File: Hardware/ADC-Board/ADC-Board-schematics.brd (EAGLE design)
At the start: 80 x 50 mm, 20 parts

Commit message: layouts
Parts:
- removed CDCS502: CDCS502, components:SSOP-8
- removed IC6: (no value), SparkFun-PowerIC:SOT23-5
- added U$1: CDCS502TSSOP-8, components:TSSOP-8
- added U1: (no value), SparkFun-PowerIC:SOT223
- C28: value (none) -> 10uF
- moved TLV71333 5.08 mm to (18.7, 18.7)
- moved C27 5.08 mm to (14.2, 18.8)
- moved JP1 5.08 mm to (10.2, 25.4)
- moved C28 5.08 mm to (16.7, 25.8)
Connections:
- net +12VDC: now also U1.3; no longer IC6.3, IC6.4
- net 3V3: now also U$1.7; no longer CDCS502.7
- net 5VCC: now also U1.2, U1.4; no longer IC6.5
- net GND: now also U$1.2, U$1.3, U$1.4, U$1.5, U1.1; no longer CDCS502.2, CDCS502.3, CDCS502.4, CDCS502.5, IC6.2
- net N$29: now also U$1.1; no longer CDCS502.1
- net N$30: now also U$1.8; no longer CDCS502.8
- net N$32: now also U$1.6; no longer CDCS502.6
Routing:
- net 3V3: track 42.3 -> 48.9 mm
- net GND: track 205.3 -> 210.8 mm
- net 5VCC: track 18.8 -> 24.0 mm
- net 5VCON: track 11.8 -> 16.1 mm
- net N$30: track 6.68 -> 8.62 mm
- net N$32: track 12.6 -> 11.1 mm
- net +12VDC: track 10.8 -> 9.75 mm

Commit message: tvs considerations
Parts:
- added D1, D2, D3, D4, D5: (no value), diode:DO-214AC
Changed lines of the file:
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@@
 </element>
 <element name="U$1" library="components" package="TSSOP-8" value="CDCS502TSSOP-8" x="45.42" y="13.57" rot="R180"/>
+<element name="D1" library="diode" package="DO-214AC" value="" x="9.51" y="5.79"/>
+<element name="D2" library="diode" package="DO-214AC" value="" x="3.81" y="-3.81"/>
+<element name="D3" library="diode" package="DO-214AC" value="" x="3.81" y="-8.89"/>
+<element name="D4" library="diode" package="DO-214AC" value="" x="3.81" y="-13.97"/>
+<element name="D5" library="diode" package="DO-214AC" value="" x="3.81" y="-19.05"/>
 </elements>
 <signals>

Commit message: adc-board
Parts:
- moved JP1 24.3 mm to (-6.35, 7.62)
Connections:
- net 5VCC: now also C27.1, TLV71333.1, TLV71333.3
- net 5VCON: no longer C27.1, TLV71333.1, TLV71333.3
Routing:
- net GND: track 210.8 -> 169.2 mm
- net 5VCON: track 16.1 -> 3.69 mm
- net +12VDC: track 9.75 -> 4.40 mm
- net 5VCC: track 24.0 -> 28.2 mm
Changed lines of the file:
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@@
 <layer number="14" name="Route14" color="1" fill="6" visible="no" active="no"/>
 <layer number="15" name="Route15" color="4" fill="6" visible="no" active="no"/>
-<layer number="16" name="Bottom" color="1" fill="1" visible="no" active="yes"/>
+<layer number="16" name="Bottom" color="1" fill="1" visible="yes" active="yes"/>
 <layer number="17" name="Pads" color="2" fill="1" visible="yes" active="yes"/>
 <layer number="18" name="Vias" color="2" fill="1" visible="yes" active="yes"/>
@@
 <layer number="24" name="bOrigins" color="15" fill="1" visible="yes" active="yes"/>
 <layer number="25" name="tNames" color="7" fill="1" visible="yes" active="yes"/>
-<layer number="26" name="bNames" color="7" fill="1" visible="no" active="yes"/>
+<layer number="26" name="bNames" color="7" fill="1" visible="yes" active="yes"/>
 <layer number="27" name="tValues" color="7" fill="1" visible="no" active="yes"/>
 <layer number="28" name="bValues" color="7" fill="1" visible="no" active="yes"/>
@@
 <element name="JP4" library="pinhead" package="2X02" value="" x="68.58" y="34.29" rot="R270"/>
 <element name="PCM1808" library="Pekkas_libraries" package="R-PDSO-G14" value="PCM1808PW" x="46.99" y="22.86"/>
-<element name="JP1" library="pinhead" package="2X02" value="" x="10.16" y="25.4"/>
+<element name="JP1" library="pinhead" package="2X02" value="" x="-6.35" y="7.62"/>
 <element name="TLV71333" library="Pekkas_libraries" package="SOT23-5" value="TVL713" x="18.74" y="18.68" rot="R270"/>
 <element name="C1" library="rcl" package="C0603" value="0.1uF" x="45.7" y="16.81"/>
@@
 <wire x1="47.85" y1="32.89" x2="47.72" y2="33.02" width="0.8128" layer="1"/>
 <contactref element="JP1" pad="4"/>
-<wire x1="11.43" y1="26.67" x2="13.12" y2="26.67" width="1.6764" layer="1"/>
-<wire x1="13.12" y1="26.67" x2="13.77" y2="27.32" width="1.6764" layer="1"/>
-<wire x1="13.77" y1="27.32" x2="13.97" y2="27.32" width="1.6764" layer="1"/>
-<wire x1="13.97" y1="27.32" x2="16.56" y2="27.32" width="1.6764" layer="1"/>
-<wire x1="34.29" y1="29.94" x2="21.59" y2="29.94" width="1.6764" layer="1"/>
-<wire x1="21.59" y1="29.94" x2="16.59" y2="29.94" width="1.6764" layer="1"/>
-<wire x1="16.59" y1="29.94" x2="13.97" y2="27.32" width="1.6764" layer="1"/>
 <contactref element="JP1" pad="2"/>
-<wire x1="11.43" y1="26.67" x2="8.89" y2="26.67" width="1.6764" layer="1"/>
+<wire x1="-5.08" y1="8.89" x2="-7.62" y2="8.89" width="1.6764" layer="1"/>
 <wire x1="14.19" y1="17.94" x2="14.13" y2="17.94" width="0.8128" layer="1"/>
 <wire x1="14.13" y1="17.94" x2="13.97" y2="17.78" width="0.8128" layer="1"/>
@@
 <wire x1="12.93" y1="17.78" x2="12.77" y2="17.62" width="1" layer="1"/>
 <wire x1="12.77" y1="17.62" x2="7.78" y2="17.62" width="1.6764" layer="1"/>
-<wire x1="7.78" y1="17.62" x2="5.08" y2="20.32" width="1.6764" layer="1"/>
-<wire x1="5.08" y1="20.32" x2="5.08" y2="25.4" width="1.6764" layer="1"/>
-<wire x1="5.08" y1="25.4" x2="6.35" y2="26.67" width="1.6764" layer="1"/>
-<wire x1="6.35" y1="26.67" x2="8.89" y2="26.67" width="1.6764" layer="1"/>
 <wire x1="17.4399" y1="18.68" x2="15.93" y2="18.68" width="0.55" layer="1"/>
 <wire x1="15.93" y1="18.68" x2="15.17" y2="17.92" width="0.55" layer="1"/>
@@
 <contactref element="U1" pad="1"/>
 <contactref element="C28" pad="2"/>
-<wire x1="21.0312" y1="28.9814" x2="21.59" y2="28.9814" width="0.4064" layer="1"/>
-<wire x1="21.59" y1="28.9814" x2="21.59" y2="29.94" width="0.4064" layer="1"/>
 <wire x1="14.19" y1="17.94" x2="14.19" y2="17.56" width="1.016" layer="1"/>
 <wire x1="14.19" y1="17.56" x2="16.51" y2="15.24" width="1.016" layer="1"/>
@@
 <wire x1="48.295" y1="14.545" x2="48.295" y2="16.765" width="0.6096" layer="1"/>
 <wire x1="48.295" y1="16.765" x2="48.35" y2="16.82" width="0.6096" layer="1"/>
-<wire x1="16.56" y1="27.32" x2="16.66" y2="27.22" width="0" layer="19" extent="1-1"/>
+<wire x1="16.66" y1="27.22" x2="21.0312" y2="28.9814" width="0" layer="19" extent="1-1"/>
+<wire x1="17.4399" y1="18.68" x2="16.66" y2="27.22" width="0" layer="19" extent="1-1"/>
+<wire x1="27.94" y1="17.78" x2="27.66" y2="18.01" width="0" layer="19" extent="1-1"/>
+<wire x1="-5.08" y1="8.89" x2="7.78" y2="17.62" width="0" layer="19" extent="1-1"/>
 </signal>
 <signal name="+12VDC">
 <contactref element="C28" pad="1"/>
 <contactref element="JP1" pad="3"/>
-<wire x1="11.43" y1="24.13" x2="16.37" y2="24.13" width="1.6764" layer="1"/>
-<wire x1="16.37" y1="24.13" x2="16.66" y2="24.42" width="1.6764" layer="1"/>
 <contactref element="U1" pad="3"/>
 <wire x1="21.0312" y1="24.3586" x2="16.7214" y2="24.3586" width="1.27" layer="1"/>
 <wire x1="16.7214" y1="24.3586" x2="16.66" y2="24.42" width="1.27" layer="1"/>
+<wire x1="-5.08" y1="6.35" x2="16.7214" y2="24.3586" width="0" layer="19" extent="1-1"/>
 </signal>
 <signal name="5VCON">
-<contactref element="C27" pad="1"/>
-<contactref element="TLV71333" pad="1"/>
-<contactref element="TLV71333" pad="3"/>
 <contactref element="JP1" pad="1"/>
-<wire x1="8.89" y1="24.13" x2="8.89" y2="22.86" width="1.6764" layer="1"/>
-<wire x1="8.89" y1="22.86" x2="11.43" y2="20.32" width="1.6764" layer="1"/>
+<wire x1="-7.62" y1="6.35" x2="8.89" y2="22.86" width="0" layer="19" extent="1-16"/>
+<wire x1="8.89" y1="22.86" x2="11.43" y2="20.32" width="0" layer="19" extent="1-16"/>
 <wire x1="11.43" y1="20.32" x2="13.97" y2="20.32" width="1.6764" layer="1"/>
 <wire x1="13.97" y1="20.32" x2="13.97" y2="20.12" width="0.8128" layer="1"/>
 <wire x1="13.97" y1="20.12" x2="13.97" y2="19.86" width="0.8128" layer="1"/>
-<wire x1="13.97" y1="19.86" x2="14.19" y2="19.64" width="0.8128" layer="1"/>
-<wire x1="17.4399" y1="19.63" x2="14.46" y2="19.63" width="0.55" layer="1"/>
 <wire x1="14.46" y1="19.63" x2="13.97" y2="20.12" width="0.55" layer="1"/>
-<wire x1="17.4399" y1="17.73" x2="18.53" y2="17.73" width="0.4064" layer="1"/>
-<wire x1="18.53" y1="17.73" x2="18.8" y2="18" width="0.4064" layer="1"/>
-<wire x1="18.8" y1="18" x2="18.8" y2="19.2" width="0.4064" layer="1"/>
-<wire x1="18.8" y1="19.2" x2="18.4" y2="19.6" width="0.4064" layer="1"/>
-<wire x1="18.4" y1="19.6" x2="17.4699" y2="19.6" width="0.4064" layer="1"/>
-<wire x1="17.4699" y1="19.6" x2="17.4399" y2="19.63" width="0.4064" layer="1"/>
 </signal>
 <signal name="3V3">
@@
 <wire x1="27.559" y1="26.34" x2="27.229" y2="26.67" width="0.8128" layer="1"/>
 <wire x1="27.229" y1="26.67" x2="21.0312" y2="26.67" width="0.8128" layer="1"/>
+<contactref element="C27" pad="1"/>
+<contactref element="TLV71333" pad="1"/>
+<contactref element="TLV71333" pad="3"/>
+<wire x1="17.4399" y1="17.73" x2="18.53" y2="17.73" width="0.4064" layer="1"/>
+<wire x1="18.53" y1="17.73" x2="18.8" y2="18" width="0.4064" layer="1"/>
+<wire x1="18.8" y1="18" x2="18.8" y2="19.2" width="0.4064" layer="1"/>
+<wire x1="18.8" y1="19.2" x2="18.4" y2="19.6" width="0.4064" layer="1"/>
+<wire x1="18.4" y1="19.6" x2="17.4699" y2="19.6" width="0.4064" layer="1"/>
+<wire x1="17.4699" y1="19.6" x2="17.4399" y2="19.63" width="0.4064" layer="1"/>
+<wire x1="18.4" y1="19.6" x2="21.0312" y2="26.67" width="0" layer="19" extent="1-1"/>
+<wire x1="14.19" y1="19.64" x2="17.4399" y2="19.63" width="0" layer="19" extent="1-1"/>
 </signal>
 <signal name="N$31">

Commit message: HW
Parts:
- added U$2, U$3: 3MM5-PLUG, Pekkas_libraries:3MM5-PLUG
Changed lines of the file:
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@@
 <element name="D4" library="diode" package="DO-214AC" value="" x="3.81" y="-13.97"/>
 <element name="D5" library="diode" package="DO-214AC" value="" x="3.81" y="-19.05"/>
+<element name="U$2" library="Pekkas_libraries" package="3MM5-PLUG" value="3MM5-PLUG" x="77.65" y="20.52"/>
+<element name="U$3" library="Pekkas_libraries" package="3MM5-PLUG" value="3MM5-PLUG" x="77.95" y="9.05"/>
 </elements>
 <signals>

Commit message: some hw changes
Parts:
- added C2, C3: 82pF, SparkFun-Passives:0603-CAP
- added C4, VAR1, VAR2: (no value), SparkFun-Passives:0603-CAP
- added R10, R5: 20, SparkFun-Passives:0603-RES
- added R2, R7: (no value), SparkFun-Passives:0603-RES
- added R3, R4, R8, R9: 4k7, SparkFun-Passives:0603-RES
- added U2: OPA2348AIDCNTG4, Pekkas_libraries:SOT65P280X145-8N
- renumbered U$2 to IN-R, U$3 to IN-L
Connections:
- removed net N$28: C25.1, PCM1808.13
- removed net N$36: C24.2, JP4.1
- removed net N$37: C25.2, JP4.3
- new net AGND: C2.2, C3.2, C4.2, IN-L.GND, IN-R.GND, R2.1, R3.1, R7.2, R9.2, U2.4, VAR1.2, VAR2.2
- new net N$10: R10.2, U2.6, U2.7
- new net N$11: C2.1, PCM1808.14, R10.1
- new net N$12: IN-R.+, JP4.1
- new net N$13: IN-L.+, JP4.3
- new net N$5: C24.1, R3.2, R4.1, U2.5, VAR2.1
- new net N$6: R5.1, U2.1, U2.2
- new net N$7: C3.1, PCM1808.13, R5.2
- new net N$8: C25.2, R7.1
- new net N$9: C25.1, R8.2, R9.1, U2.3, VAR1.1
- net 5VCC: now also C4.1, R4.2, R8.1, U2.8
- net N$3: now also C24.2, R2.2; no longer C24.1, PCM1808.14
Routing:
- net N$3: track 15.3 -> 0.00 mm
- net N$28: track 9.94 -> 0.00 mm
- net N$37: track 7.20 -> 0.00 mm
- net N$36: track 6.15 -> 0.00 mm

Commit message: HW
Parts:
- removed D1, D2, D3, D4, D5: (no value), diode:DO-214AC
- added POT1, POT2: TRIMPOT-PVZ2A, SparkFun-Resistors:PVZ2A
- added VAR3, VAR4, VAR5: (no value), SparkFun-Passives:0603-CAP
- moved VAR2 127.2 mm to (50.8, 41.9), turned to 90 degrees
- moved VAR1 120.4 mm to (48.3, 38.1), turned to 180 degrees
- moved C4 112.4 mm to (52.1, 29.2), turned to 90 degrees
- moved C3 104.3 mm to (50.8, 22.9)
- moved C2 100.8 mm to (52.1, 20.3)
- moved R8 99.0 mm to (57.1, 34.3), turned to 90 degrees
- moved R9 97.6 mm to (53.3, 33.0), turned to 90 degrees
- moved R4 93.5 mm to (54.6, 39.4), turned to 90 degrees
- moved R10 91.6 mm to (55.9, 20.3)
- moved R5 85.4 mm to (55.9, 24.1)
- moved R7 85.4 mm to (35.6, 35.6), turned to 90 degrees
- moved R3 83.6 mm to (48.3, 34.3), turned to 90 degrees
- moved R2 80.0 mm to (35.6, 41.9), turned to 90 degrees
- moved IN-R 73.1 mm to (8.69, 44.6), turned to 90 degrees
- moved IN-L 61.7 mm to (27.8, 44.9), turned to 90 degrees
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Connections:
- removed net N$12: IN-R.+, JP4.1
- removed net N$13: IN-L.+, JP4.3
- new net N$20: IN-L.+, JP4.3, POT2.2
- new net N$21: IN-R.+, JP4.1, POT1.2
- net GND: now also VAR3.2, VAR4.2, VAR5.2
- net N$1: now also VAR4.1
- net N$2: now also VAR5.1
- net N$3: now also POT1.3
- net N$4: now also VAR3.1
- net N$8: now also POT2.3
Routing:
- net GND: track 169.2 -> 136.4 mm
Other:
- board size 80 x 50 mm -> 60.6 x 47.7 mm

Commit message: Layout and parts
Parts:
- added C5: 10uF, rcl:RADIALCAN4MM
- added U3: (no value), SparkFun-PowerIC:SOT223
- moved R2 25.5 mm to (10.2, 44.5), turned to 270 degrees
- moved C27 15.8 mm to (22.9, 3.81)
- moved TLV71333 15.3 mm to (27.6, 4.71)
- moved R8 14.5 mm to (43.2, 38.1), turned to 270 degrees
- moved POT2 13.5 mm to (22.9, 38.1), turned to 90 degrees
- moved R7 12.6 mm to (26.7, 44.5)
- moved R4 12.5 mm to (43.2, 44.5)
- moved C26 12.0 mm to (31.5, 4.89)
- moved VAR2 11.7 mm to (39.4, 44.5)
- moved POT1 9.92 mm to (7.62, 38.1), turned to 90 degrees
- moved C29 9.67 mm to (34.3, 25.4), turned to 90 degrees
- moved C2 9.25 mm to (43.2, 22.9), turned to 180 degrees
- moved R10 9.25 mm to (47.0, 22.9), turned to 90 degrees
- moved VAR1 9.25 mm to (39.4, 35.6), turned to 270 degrees
- moved C3 8.03 mm to (43.2, 25.4), turned to 180 degrees
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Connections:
- removed net 5VCON: JP1.1
- new net 5VDD: C27.1, C5.1, TLV71333.1, TLV71333.3, U3.2, U3.4
- new net 5VREF: C4.1, U2.8
- net +12VDC: now also JP1.1, U3.3
- net 5VCC: no longer C27.1, C4.1, TLV71333.1, TLV71333.3, U2.8
- net GND: now also C5.2, U3.1
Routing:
- net GND: track 136.4 -> 175.8 mm, vias 2 -> 3
- net 5VDD: track 0.00 -> 26.7 mm
- net +12VDC: track 4.40 -> 18.1 mm
- net N$31: track 8.99 -> 1.60 mm
- net 5VCC: track 28.2 -> 23.4 mm
- net 5VCON: track 3.69 -> 0.00 mm
- net 3V3: track 48.9 -> 45.8 mm, vias 2 -> 0

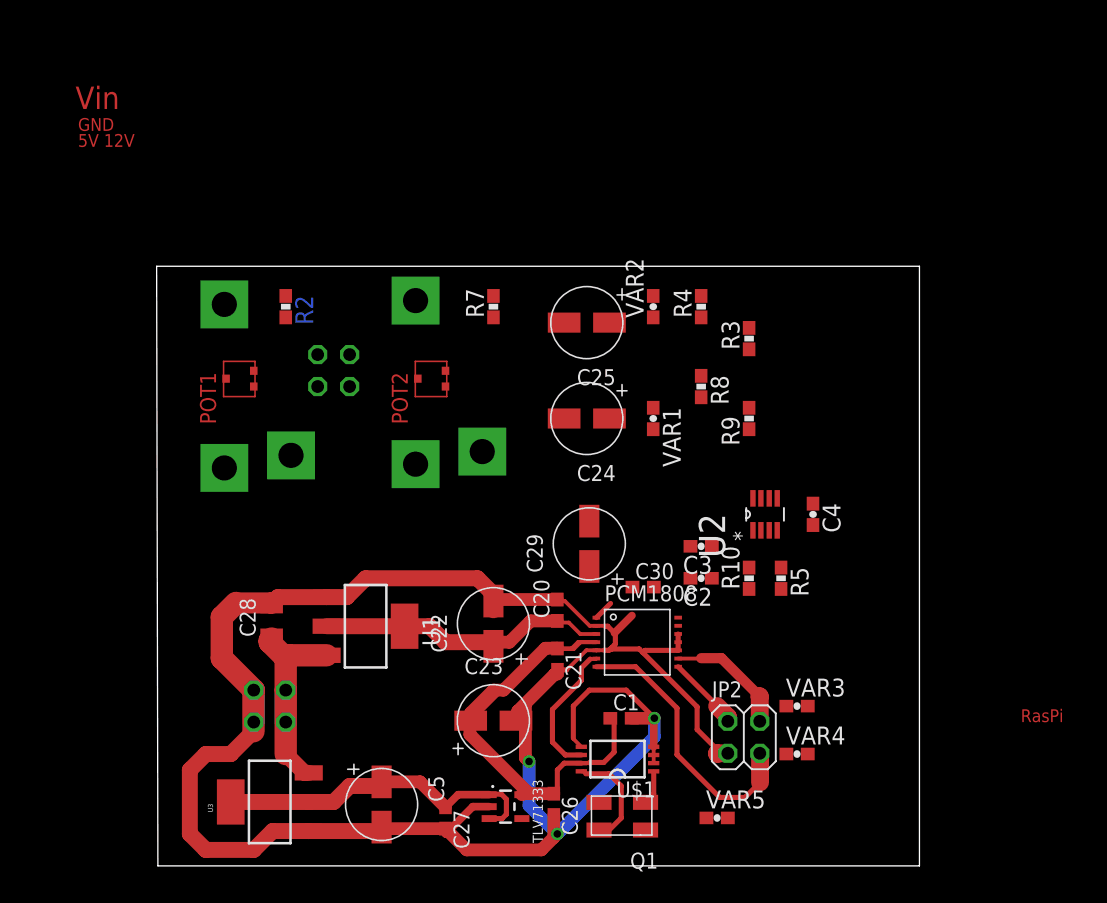
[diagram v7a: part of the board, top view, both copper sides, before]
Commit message: ADC-board layout
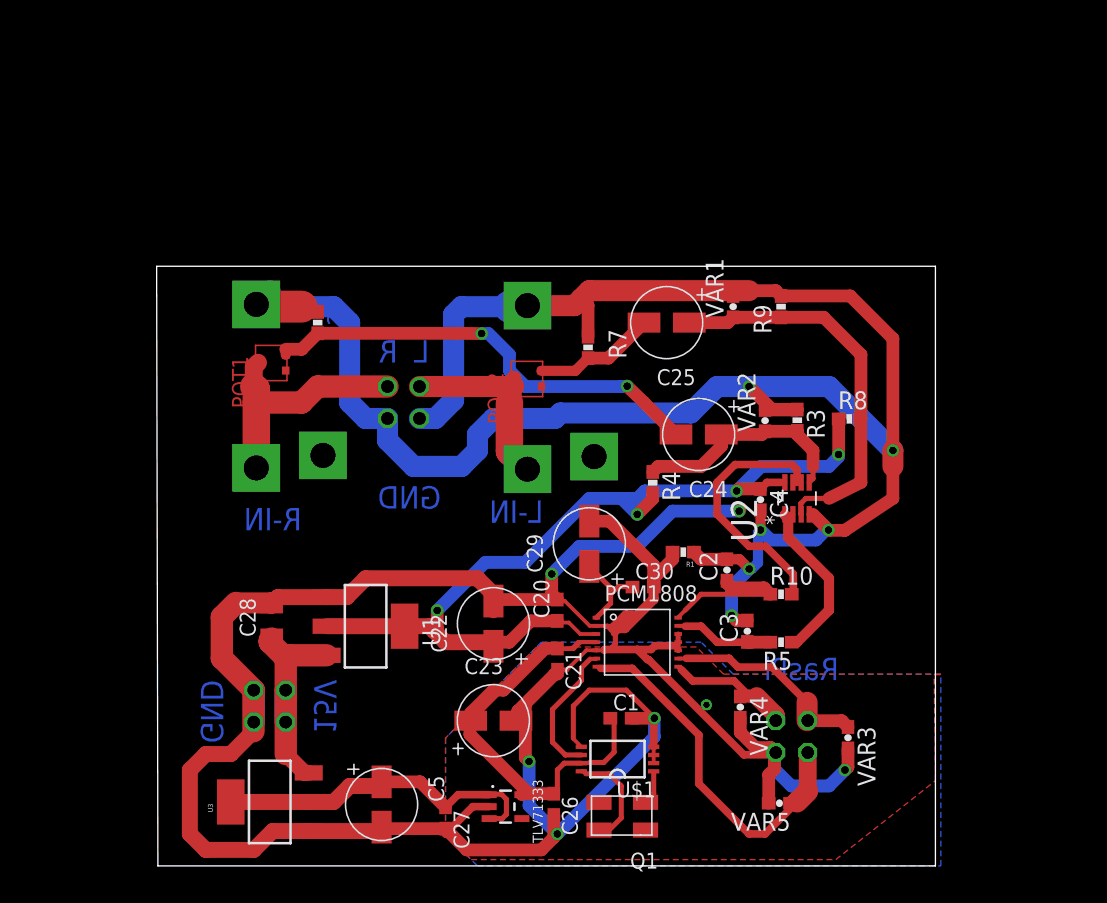
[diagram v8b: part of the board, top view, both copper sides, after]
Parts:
- added R1: 0, SparkFun-Passives:0603-RES
- moved R4 14.5 mm to (39.3, 30.5), turned to 270 degrees
- moved VAR2 12.7 mm to (48.3, 35.4)
- moved R8 12.1 mm to (55.0, 35.5), turned to 0 degrees
- moved VAR1 10.9 mm to (45.7, 44.5), turned to 90 degrees
- moved R9 9.25 mm to (49.5, 44.5)
- moved C24 8.98 mm to (43.2, 34.3)
- moved IN-L 8.90 mm to (29.4, 44.5)
- moved R7 8.19 mm to (34.2, 41.2)
- moved C3 7.68 mm to (46.9, 18.6), turned to 90 degrees
- moved POT2 7.62 mm to (30.5, 38.1)
- moved R3 7.54 mm to (50.8, 35.4), turned to 270 degrees
- moved C25 6.35 mm to (40.6, 43.2)
- moved JP4 6.10 mm to (19.5, 36.8)
- moved VAR4 5.85 mm to (46.3, 12.6), turned to 270 degrees
- moved VAR5 5.09 mm to (49.4, 4.98), turned to 180 degrees
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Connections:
- removed net 5VREF: C4.1, U2.8
- removed net N$2: JP2.3, PCM1808.7, VAR5.1
- new net N$12: JP2.4, PCM1808.7, VAR5.1
- net 5VCC: now also C4.1, U2.8
- net AGND: now also JP4.2, JP4.4, R1.1
- net GND: now also JP2.2, R1.2; no longer JP2.1, JP4.2
- net N$1: now also JP2.1; no longer JP2.2
- net N$4: now also JP2.3; no longer JP2.4
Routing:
- net AGND: track 0.00 -> 176.6 mm, vias 0 -> 6
- net GND: track 175.8 -> 237.9 mm, vias 3 -> 6
- net 5VCC: track 23.4 -> 73.2 mm, vias 0 -> 4
- net N$3: track 0.00 -> 36.1 mm, vias 0 -> 2
- net N$9: track 0.00 -> 31.4 mm
- net N$12: track 0.00 -> 29.6 mm
- net N$2: track 22.3 -> 0.00 mm, vias 0 -> 1
- net N$10: track 0.00 -> 21.1 mm
- net N$21: track 0.00 -> 19.5 mm
- net N$5: track 0.00 -> 18.1 mm
- net N$20: track 0.00 -> 15.4 mm
- net N$6: track 0.00 -> 13.7 mm
- net N$11: track 0.00 -> 12.1 mm
- net N$8: track 0.00 -> 10.1 mm
- net N$7: track 0.00 -> 8.02 mm
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- added copper zone on layer 1, net GND
- added copper zone on layer 16, net GND
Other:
- board size 60.6 x 47.7 mm -> 61.9 x 47.7 mm
- board text added: "15V"
- board text added: "L"
- board text added: "L-IN"
- board text added: "R"
- board text added: "R-IN"
- board text removed: "5V 12V"
- board text removed: "Vin"
